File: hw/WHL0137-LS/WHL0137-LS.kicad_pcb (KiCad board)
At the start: 2 copper layers, 109.4 x 133.5 mm, 91 parts, among them J1 Conn_01x05, U1 IS31FL3236A, U2 IS31FL3236A

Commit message: Some floor planning
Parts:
- moved C2 136.4 mm to (-25.4, -62.5), turned to 90 degrees
- moved JP2 128.8 mm to (-20.3, -66.0)
- moved JP1 124.2 mm to (-20.3, -68.6)
- moved C1 111.1 mm to (-11.1, -66.0)
- moved R1 106.8 mm to (-4.72, -54.6)
- moved R2 106.8 mm to (-4.72, -57.6)
- moved R3 76.1 mm to (12.7, -59.7)
- moved R4 73.3 mm to (11.5, -56.9)
- moved C3 71.3 mm to (11.5, -53.3)
- moved TP1 63.1 mm to (5.82, -55.9)
- moved TP2 63.1 mm to (1.27, -55.9)
- moved C4 58.5 mm to (25.4, -62.2), turned to 90 degrees
- moved JP4 57.8 mm to (20.3, -66.0)
- moved R5 32.7 mm to (11.8, -63.5)
- moved D73 28.0 mm to (11.8, -66.0)
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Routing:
- net Net-(U2-Pad40): track 0.00 -> 9.06 mm
- net Net-(U1-Pad40): track 0.00 -> 9.06 mm
- net +5V: track 0.00 -> 5.78 mm, vias 0 -> 3
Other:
- board size 109.4 x 133.5 mm -> 111.5 x 124.3 mm
- copper layers 2 -> 4

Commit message: Some layout
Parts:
- removed R5: 510, Resistor_SMD:R_0805_2012Metric
- R1: value 100k -> 510
- R2: value 3.3k -> 100k
- R3: value 100k -> 3.3k
- moved R3 47.6 mm to (-32.8, -73.7), turned to 90 degrees
- moved TP1 41.4 mm to (-35.6, -55.9)
- moved TP2 41.4 mm to (-40.1, -55.9)
- moved R2 22.7 mm to (-26.7, -63.2), turned to 90 degrees
- moved JP2 21.2 mm to (-4.32, -52.1)
- moved JP1 21.2 mm to (-4.32, -54.6)
- moved JP4 21.1 mm to (4.57, -52.1)
- moved JP3 21.1 mm to (4.57, -54.6)
- moved C2 11.8 mm to (-17.0, -70.9), turned to 0 degrees
- moved C1 6.54 mm to (-17.0, -68.8)
- moved R1 5.18 mm to (-6.60, -59.4), turned to 90 degrees
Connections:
- D1 pad 1: Net-(U1-Pad47) -> Net-(D1-Pad1)
- D2 pad 1: Net-(U1-Pad48) -> Net-(D2-Pad1)
- D28 pad 1: Net-(U1-Pad38) -> Net-(D28-Pad1)
- D29 pad 1: Net-(U1-Pad37) -> Net-(D29-Pad1)
- D3 pad 1: Net-(U1-Pad1) -> Net-(D3-Pad1)
- D37 pad 1: Net-(U2-Pad8) -> Net-(D37-Pad1)
- D38 pad 1: Net-(U2-Pad7) -> Net-(D38-Pad1)
- D39 pad 1: Net-(U2-Pad6) -> Net-(D39-Pad1)
- D4 pad 1: Net-(U1-Pad2) -> Net-(D4-Pad1)
- D40 pad 1: Net-(U2-Pad5) -> Net-(D40-Pad1)
- D41 pad 1: Net-(U2-Pad3) -> Net-(D41-Pad1)
- D42 pad 1: Net-(U2-Pad2) -> Net-(D42-Pad1)
- D43 pad 1: Net-(U2-Pad1) -> Net-(D43-Pad1)
- D44 pad 1: Net-(U2-Pad48) -> Net-(D44-Pad1)
- D45 pad 1: Net-(U2-Pad47) -> Net-(D45-Pad1)
- D5 pad 1: Net-(U1-Pad3) -> Net-(D5-Pad1)
- D6 pad 1: Net-(U1-Pad5) -> Net-(D6-Pad1)
- D7 pad 1: Net-(U1-Pad6) -> Net-(D7-Pad1)
- D8 pad 1: Net-(U1-Pad7) -> Net-(D8-Pad1)
- D9 pad 1: Net-(U1-Pad8) -> Net-(D9-Pad1)
- R1 pad 1: GND -> +5V
- R1 pad 2: /inner_LED_ring/SDB -> Net-(D73-Pad2)
- R2 pad 1: Net-(U1-Pad44) -> /inner_LED_ring/SDB
- R3 pad 1: GND -> Net-(R3-Pad1)
- R3 pad 2: /inner_LED_ring/SDB -> GND
- U1 pad 1: Net-(U1-Pad1) -> Net-(D14-Pad1)
- U1 pad 10: Net-(D11-Pad1) -> Net-(D5-Pad1)
- U1 pad 11: Net-(D12-Pad1) -> Net-(D7-Pad1)
- U1 pad 12: Net-(D13-Pad1) -> Net-(D9-Pad1)
- U1 pad 13: Net-(D14-Pad1) -> Net-(D11-Pad1)
- U1 pad 14: Net-(D15-Pad1) -> Net-(D13-Pad1)
- U1 pad 15: Net-(D16-Pad1) -> Net-(D15-Pad1)
- U1 pad 17: Net-(D18-Pad1) -> Net-(D19-Pad1)
- U1 pad 2: Net-(U1-Pad2) -> Net-(D12-Pad1)
- U1 pad 20: Net-(D19-Pad1) -> Net-(D20-Pad1)
- U1 pad 21: Net-(D20-Pad1) -> Net-(D22-Pad1)
- U1 pad 22: Net-(D21-Pad1) -> Net-(D24-Pad1)
- U1 pad 23: Net-(D22-Pad1) -> Net-(D26-Pad1)
- U1 pad 24: Net-(D23-Pad1) -> Net-(D28-Pad1)
- U1 pad 25: Net-(D24-Pad1) -> Net-(D30-Pad1)
- U1 pad 26: Net-(D25-Pad1) -> Net-(D32-Pad1)
- U1 pad 27: Net-(D26-Pad1) -> Net-(D34-Pad1)
- U1 pad 28: Net-(D27-Pad1) -> Net-(D36-Pad1)
- U1 pad 29: Net-(D36-Pad1) -> Net-(D37-Pad1)
- U1 pad 3: Net-(U1-Pad3) -> Net-(D10-Pad1)
- U1 pad 31: Net-(D34-Pad1) -> Net-(D33-Pad1)
- U1 pad 32: Net-(D33-Pad1) -> Net-(D31-Pad1)
- U1 pad 34: Net-(D32-Pad1) -> Net-(D29-Pad1)
- U1 pad 35: Net-(D31-Pad1) -> Net-(D27-Pad1)
- U1 pad 36: Net-(D30-Pad1) -> Net-(D25-Pad1)
- U1 pad 37: Net-(U1-Pad37) -> Net-(D23-Pad1)
- U1 pad 38: Net-(U1-Pad38) -> Net-(D21-Pad1)
- U1 pad 44: Net-(U1-Pad44) -> Net-(R3-Pad1)
- U1 pad 47: Net-(U1-Pad47) -> Net-(D18-Pad1)
- U1 pad 48: Net-(U1-Pad48) -> Net-(D16-Pad1)
- U1 pad 5: Net-(U1-Pad5) -> Net-(D8-Pad1)
- U1 pad 6: Net-(U1-Pad6) -> Net-(D6-Pad1)
- U1 pad 7: Net-(U1-Pad7) -> Net-(D4-Pad1)
- U1 pad 8: Net-(U1-Pad8) -> Net-(D2-Pad1)
- U1 pad 9: Net-(D10-Pad1) -> Net-(D3-Pad1)
- U2 pad 1: Net-(U2-Pad1) -> Net-(D50-Pad1)
- U2 pad 10: Net-(D47-Pad1) -> Net-(D41-Pad1)
- U2 pad 11: Net-(D48-Pad1) -> Net-(D43-Pad1)
- U2 pad 12: Net-(D49-Pad1) -> Net-(D45-Pad1)
- U2 pad 13: Net-(D50-Pad1) -> Net-(D47-Pad1)
- U2 pad 14: Net-(D51-Pad1) -> Net-(D49-Pad1)
- U2 pad 15: Net-(D52-Pad1) -> Net-(D51-Pad1)
- U2 pad 17: Net-(D54-Pad1) -> Net-(D55-Pad1)
- U2 pad 2: Net-(U2-Pad2) -> Net-(D48-Pad1)
- U2 pad 20: Net-(D55-Pad1) -> Net-(D56-Pad1)
- U2 pad 21: Net-(D56-Pad1) -> Net-(D58-Pad1)
- U2 pad 22: Net-(D57-Pad1) -> Net-(D60-Pad1)
- U2 pad 23: Net-(D58-Pad1) -> Net-(D62-Pad1)
- U2 pad 24: Net-(D59-Pad1) -> Net-(D64-Pad1)
- U2 pad 25: Net-(D60-Pad1) -> Net-(D66-Pad1)
- U2 pad 26: Net-(D61-Pad1) -> Net-(D68-Pad1)
- U2 pad 27: Net-(D62-Pad1) -> Net-(D70-Pad1)
- U2 pad 28: Net-(D63-Pad1) -> Net-(D72-Pad1)
- U2 pad 29: Net-(D64-Pad1) -> Net-(D1-Pad1)
- U2 pad 3: Net-(U2-Pad3) -> Net-(D46-Pad1)
- U2 pad 30: Net-(D65-Pad1) -> Net-(D71-Pad1)
- U2 pad 31: Net-(D66-Pad1) -> Net-(D69-Pad1)
- U2 pad 34: Net-(D68-Pad1) -> Net-(D65-Pad1)
- U2 pad 35: Net-(D69-Pad1) -> Net-(D63-Pad1)
- U2 pad 36: Net-(D70-Pad1) -> Net-(D61-Pad1)
- U2 pad 37: Net-(D71-Pad1) -> Net-(D59-Pad1)
- U2 pad 38: Net-(D72-Pad1) -> Net-(D57-Pad1)
- U2 pad 47: Net-(U2-Pad47) -> Net-(D54-Pad1)
- U2 pad 48: Net-(U2-Pad48) -> Net-(D52-Pad1)
- U2 pad 5: Net-(U2-Pad5) -> Net-(D44-Pad1)
- U2 pad 6: Net-(U2-Pad6) -> Net-(D42-Pad1)
- U2 pad 7: Net-(U2-Pad7) -> Net-(D40-Pad1)
- U2 pad 8: Net-(U2-Pad8) -> Net-(D38-Pad1)
- U2 pad 9: Net-(D46-Pad1) -> Net-(D39-Pad1)
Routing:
- net Net-(D21-Pad1): track 0.00 -> 14.2 mm
- net Net-(D23-Pad1): track 0.00 -> 11.7 mm
- net Net-(D25-Pad1): track 0.00 -> 9.07 mm
- net Net-(JP3-Pad2): track 9.06 -> 0.00 mm
- net Net-(JP1-Pad2): track 9.06 -> 0.00 mm
- net Net-(D27-Pad1): track 0.00 -> 8.28 mm
- net Net-(D5-Pad1): track 0.00 -> 8.07 mm
- net Net-(D29-Pad1): track 0.00 -> 7.49 mm
- net Net-(D4-Pad1): track 0.00 -> 6.90 mm
- net Net-(D31-Pad1): track 0.00 -> 6.50 mm
- net Net-(D2-Pad1): track 0.00 -> 6.32 mm
- net /inner_LED_ring/SCL: track 0.00 -> 5.95 mm
- net +5V: track 5.78 -> 0.00 mm, vias 3 -> 0
- net Net-(D33-Pad1): track 0.00 -> 5.71 mm
- net /inner_LED_ring/SDA: track 0.00 -> 5.56 mm
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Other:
- board size 111.5 x 124.3 mm -> 153.8 x 153.8 mm

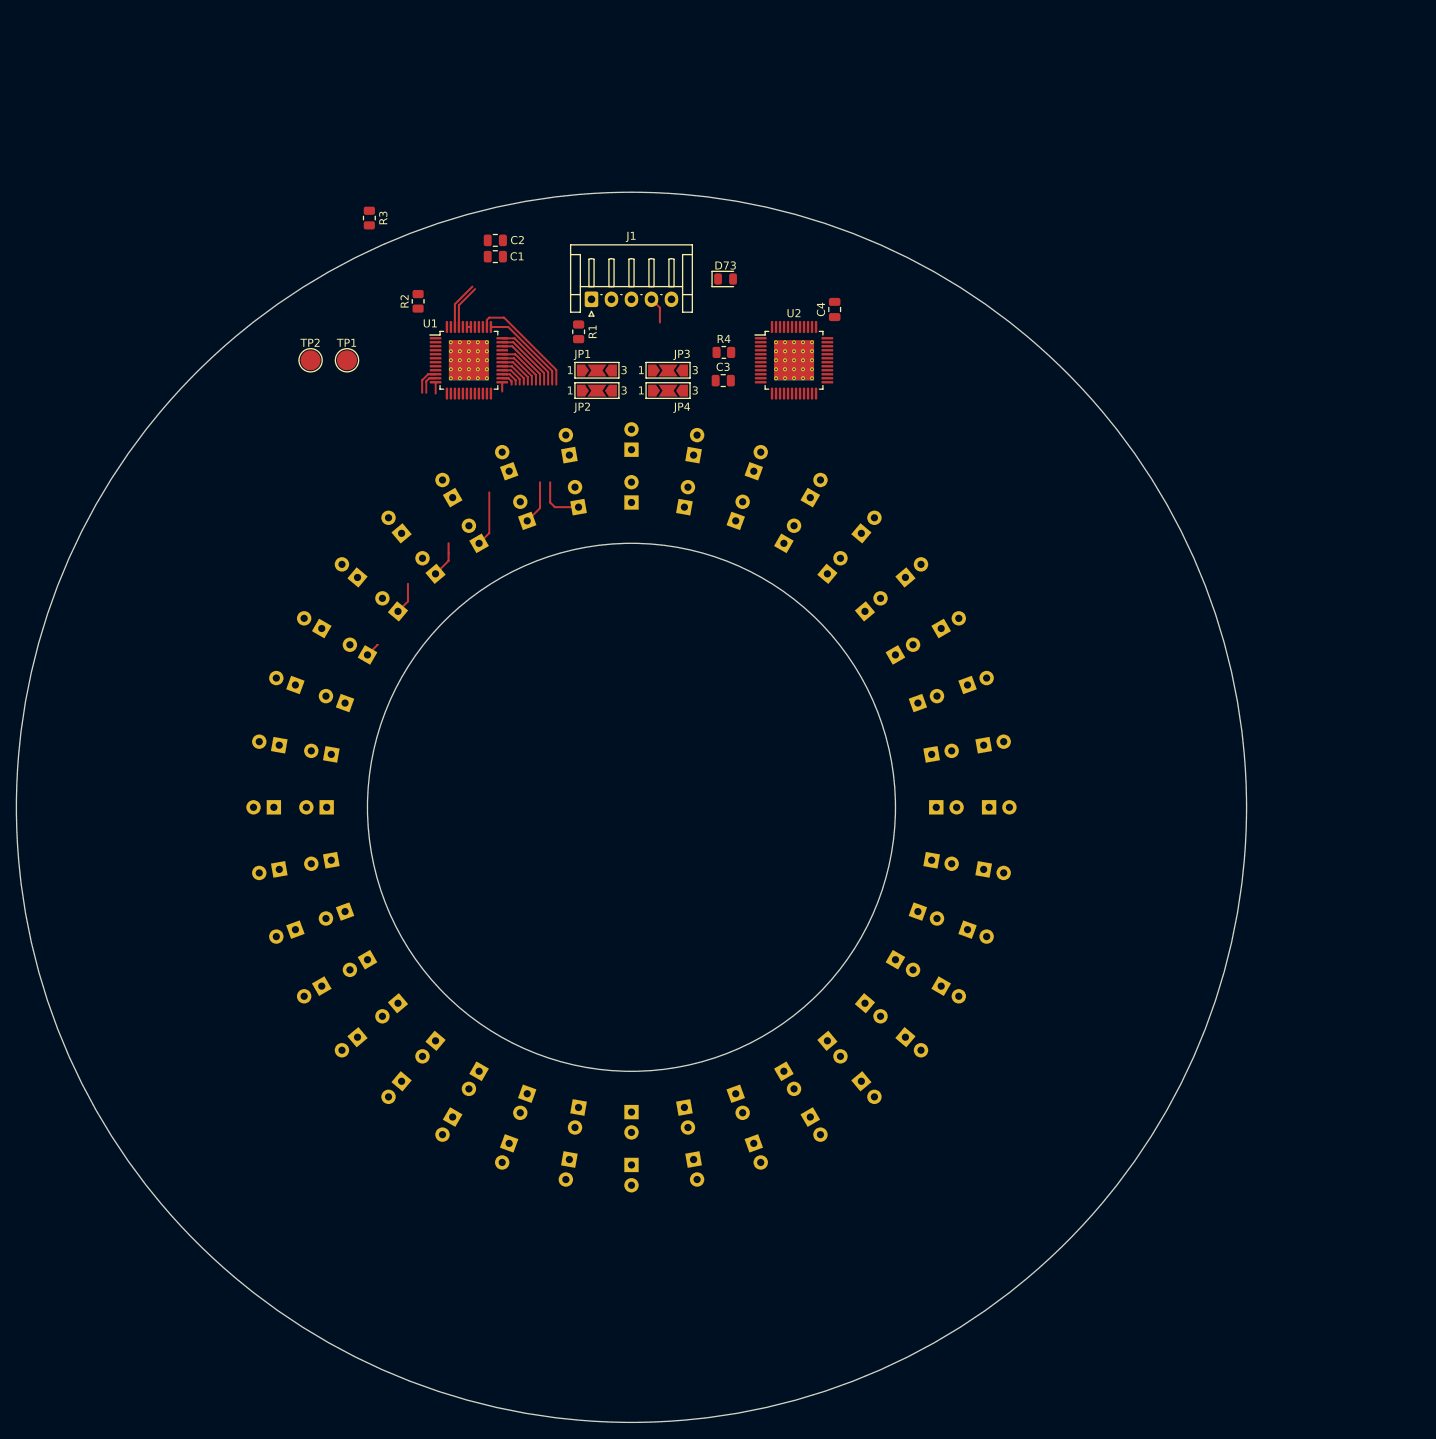
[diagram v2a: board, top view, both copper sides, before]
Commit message: Routed LED traces and fixed designators
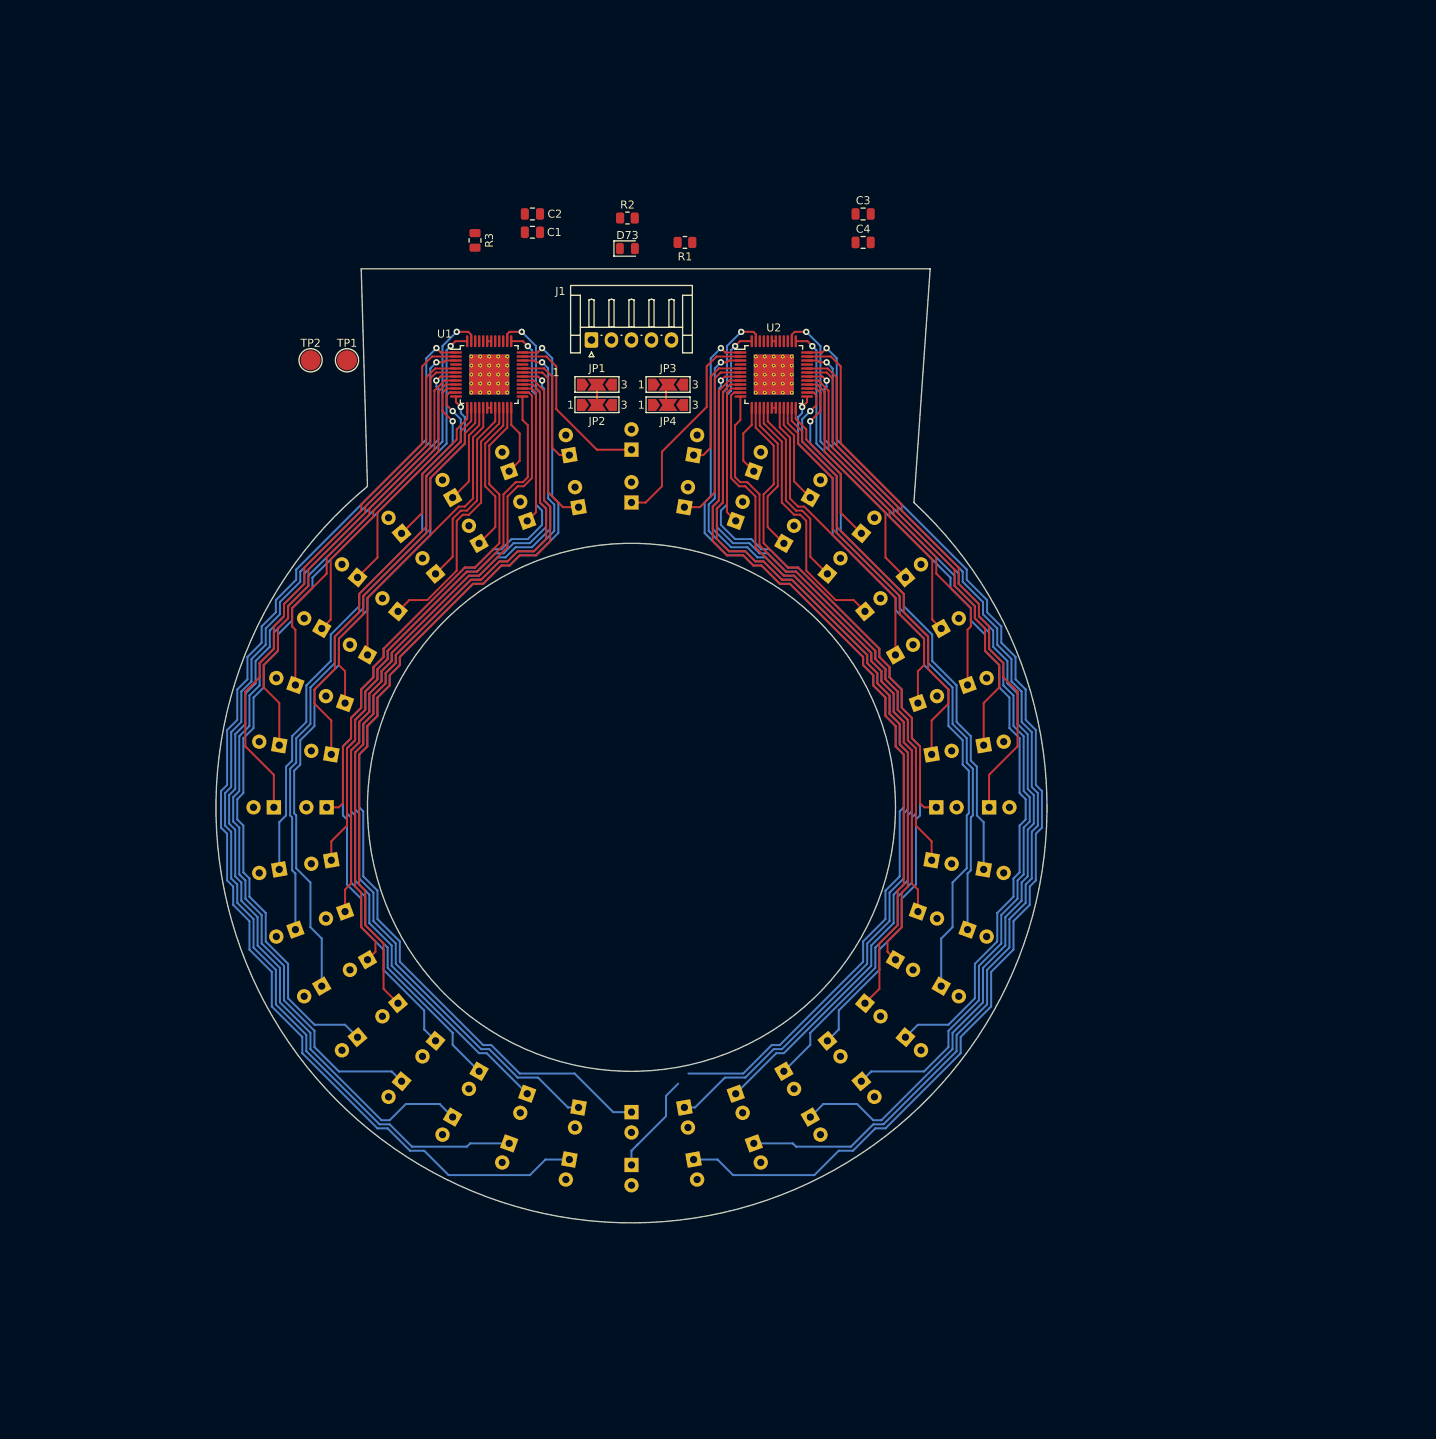
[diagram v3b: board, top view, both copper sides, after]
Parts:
- removed R4: 3.3k, Resistor_SMD:R_0805_2012Metric
- R1: value 510 -> 3.3k
- R2: value 100k -> 510
- moved R2 28.2 mm to (-0.51, -73.7), turned to 0 degrees
- moved C3 27.2 mm to (29.0, -74.2)
- moved R1 17.4 mm to (6.68, -70.6), turned to 0 degrees
- moved R3 13.5 mm to (-19.6, -70.9)
- moved D73 12.8 mm to (-0.51, -69.8)
- moved C4 9.11 mm to (29.0, -70.6), turned to 0 degrees
- moved C2 5.69 mm to (-12.4, -74.2)
- moved C1 5.55 mm to (-12.4, -71.9)
- moved J1 5.08 mm to (-5.00, -58.4)
- moved U1 3.10 mm to (-17.8, -54.1)
- moved U2 3.10 mm to (17.8, -54.1)
- moved JP1 1.78 mm to (-4.32, -52.8)
- moved JP2 1.78 mm to (-4.32, -50.3)
- moved JP3 1.78 mm to (4.57, -52.8)
- moved JP4 1.78 mm to (4.57, -50.3)
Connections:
- net /inner_LED_ring/SCL renamed /led_driver_1/SCL
- net /inner_LED_ring/SDA renamed /led_driver_1/SDA
- net Net-(JP1-Pad2) renamed /led_driver_1/AD
- net Net-(JP3-Pad2) renamed /led_driver_2/AD
- net Net-(R3-Pad1) renamed /led_driver_1/R_EXT
- J1 pad 4: /inner_LED_ring/SDB -> /led_driver_1/SDB
- R1 pad 1: +5V -> /led_driver_2/R_EXT
- R1 pad 2: Net-(D73-Pad2) -> GND
- R2 pad 1: /inner_LED_ring/SDB -> +5V
- R2 pad 2: GND -> Net-(D73-Pad2)
- U1 pad 1: Net-(D14-Pad1) -> Net-(D54-Pad1)
- U1 pad 10: Net-(D5-Pad1) -> Net-(D47-Pad1)
- U1 pad 11: Net-(D7-Pad1) -> Net-(D48-Pad1)
- U1 pad 12: Net-(D9-Pad1) -> Net-(D49-Pad1)
- U1 pad 13: Net-(D11-Pad1) -> Net-(D41-Pad1)
- U1 pad 14: Net-(D13-Pad1) -> Net-(D9-Pad1)
- U1 pad 15: Net-(D15-Pad1) -> Net-(D8-Pad1)
- U1 pad 16: Net-(D17-Pad1) -> Net-(D40-Pad1)
- U1 pad 17: Net-(D19-Pad1) -> Net-(D7-Pad1)
- U1 pad 2: Net-(D12-Pad1) -> Net-(D46-Pad1)
- U1 pad 20: Net-(D20-Pad1) -> Net-(D5-Pad1)
- U1 pad 21: Net-(D22-Pad1) -> Net-(D6-Pad1)
- U1 pad 22: Net-(D24-Pad1) -> Net-(D4-Pad1)
- U1 pad 23: Net-(D26-Pad1) -> Net-(D10-Pad1)
- U1 pad 24: Net-(D28-Pad1) -> Net-(D39-Pad1)
- U1 pad 25: Net-(D30-Pad1) -> Net-(D11-Pad1)
- U1 pad 26: Net-(D32-Pad1) -> Net-(D12-Pad1)
- U1 pad 27: Net-(D34-Pad1) -> Net-(D3-Pad1)
- U1 pad 28: Net-(D36-Pad1) -> Net-(D13-Pad1)
- U1 pad 29: Net-(D37-Pad1) -> Net-(D14-Pad1)
- U1 pad 3: Net-(D10-Pad1) -> Net-(D53-Pad1)
- U1 pad 30: Net-(D35-Pad1) -> Net-(D17-Pad1)
- U1 pad 31: Net-(D33-Pad1) -> Net-(D2-Pad1)
- U1 pad 32: Net-(D31-Pad1) -> Net-(D38-Pad1)
- U1 pad 34: Net-(D29-Pad1) -> Net-(D18-Pad1)
- U1 pad 35: Net-(D27-Pad1) -> Net-(D37-Pad1)
- U1 pad 36: Net-(D25-Pad1) -> Net-(D19-Pad1)
- U1 pad 37: Net-(D23-Pad1) -> Net-(D15-Pad1)
- U1 pad 38: Net-(D21-Pad1) -> Net-(D16-Pad1)
- U1 pad 39: /inner_LED_ring/SDB -> /led_driver_1/SDB
- U1 pad 47: Net-(D18-Pad1) -> Net-(D51-Pad1)
- U1 pad 48: Net-(D16-Pad1) -> Net-(D50-Pad1)
- U1 pad 5: Net-(D8-Pad1) -> Net-(D45-Pad1)
- U1 pad 6: Net-(D6-Pad1) -> Net-(D44-Pad1)
- U1 pad 7: Net-(D4-Pad1) -> Net-(D52-Pad1)
- U1 pad 8: Net-(D2-Pad1) -> Net-(D43-Pad1)
- U1 pad 9: Net-(D3-Pad1) -> Net-(D42-Pad1)
- U2 pad 1: Net-(D50-Pad1) -> Net-(D55-Pad1)
- U2 pad 10: Net-(D41-Pad1) -> Net-(D35-Pad1)
- U2 pad 11: Net-(D43-Pad1) -> Net-(D26-Pad1)
- U2 pad 12: Net-(D45-Pad1) -> Net-(D27-Pad1)
- U2 pad 13: Net-(D47-Pad1) -> Net-(D71-Pad1)
- U2 pad 14: Net-(D49-Pad1) -> Net-(D28-Pad1)
- U2 pad 15: Net-(D51-Pad1) -> Net-(D34-Pad1)
- U2 pad 16: Net-(D53-Pad1) -> Net-(D32-Pad1)
- U2 pad 17: Net-(D55-Pad1) -> Net-(D33-Pad1)
- U2 pad 2: Net-(D48-Pad1) -> Net-(D1-Pad1)
- U2 pad 20: Net-(D56-Pad1) -> Net-(D31-Pad1)
- U2 pad 21: Net-(D58-Pad1) -> Net-(D70-Pad1)
- U2 pad 22: Net-(D60-Pad1) -> Net-(D30-Pad1)
- U2 pad 23: Net-(D62-Pad1) -> Net-(D29-Pad1)
- U2 pad 24: Net-(D64-Pad1) -> Net-(D69-Pad1)
- U2 pad 25: Net-(D66-Pad1) -> Net-(D61-Pad1)
- U2 pad 26: Net-(D68-Pad1) -> Net-(D62-Pad1)
- U2 pad 27: Net-(D70-Pad1) -> Net-(D63-Pad1)
- U2 pad 28: Net-(D72-Pad1) -> Net-(D68-Pad1)
- U2 pad 29: Net-(D1-Pad1) -> Net-(D67-Pad1)
- U2 pad 3: Net-(D46-Pad1) -> Net-(D20-Pad1)
- U2 pad 30: Net-(D71-Pad1) -> Net-(D58-Pad1)
- U2 pad 31: Net-(D69-Pad1) -> Net-(D66-Pad1)
- U2 pad 32: Net-(D67-Pad1) -> Net-(D65-Pad1)
- U2 pad 34: Net-(D65-Pad1) -> Net-(D57-Pad1)
- U2 pad 35: Net-(D63-Pad1) -> Net-(D64-Pad1)
- U2 pad 36: Net-(D61-Pad1) -> Net-(D56-Pad1)
- U2 pad 37: Net-(D59-Pad1) -> Net-(D60-Pad1)
- U2 pad 38: Net-(D57-Pad1) -> Net-(D59-Pad1)
- U2 pad 39: /inner_LED_ring/SDB -> /led_driver_1/SDB
- U2 pad 44: Net-(R4-Pad1) -> /led_driver_2/R_EXT
- U2 pad 47: Net-(D54-Pad1) -> Net-(D22-Pad1)
- U2 pad 48: Net-(D52-Pad1) -> Net-(D23-Pad1)
- U2 pad 5: Net-(D44-Pad1) -> Net-(D72-Pad1)
- U2 pad 6: Net-(D42-Pad1) -> Net-(D36-Pad1)
- U2 pad 7: Net-(D40-Pad1) -> Net-(D21-Pad1)
- U2 pad 8: Net-(D38-Pad1) -> Net-(D24-Pad1)
- U2 pad 9: Net-(D39-Pad1) -> Net-(D25-Pad1)
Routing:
- net Net-(D56-Pad1): track 0.00 -> 146.7 mm, vias 0 -> 1
- net Net-(D54-Pad1): track 0.00 -> 146.7 mm
- net Net-(D55-Pad1): track 0.00 -> 135.4 mm
- net Net-(D57-Pad1): track 0.00 -> 134.3 mm, vias 0 -> 1
- net Net-(D53-Pad1): track 0.00 -> 134.3 mm
- net Net-(D19-Pad1): track 0.00 -> 131.9 mm, vias 0 -> 1
- net Net-(D58-Pad1): track 0.00 -> 124.4 mm, vias 0 -> 1
- net Net-(D52-Pad1): track 0.00 -> 124.4 mm, vias 0 -> 2
- net Net-(D20-Pad1): track 0.00 -> 123.6 mm
- net Net-(D18-Pad1): track 0.00 -> 123.6 mm, vias 0 -> 1
- net Net-(D59-Pad1): track 0.00 -> 120.6 mm, vias 0 -> 1
- net Net-(D51-Pad1): track 0.00 -> 120.6 mm, vias 0 -> 1
- net Net-(D22-Pad1): track 0.00 -> 116.2 mm, vias 0 -> 1
- net Net-(D16-Pad1): track 0.00 -> 116.2 mm, vias 0 -> 1
- net Net-(D17-Pad1): track 0.00 -> 114.7 mm, vias 0 -> 1
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- added copper zone on In1.Cu, net +5V
- added copper zone on In2.Cu, net +5V
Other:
- board size 153.8 x 153.8 mm -> 103.9 x 119.3 mm

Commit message: More layout progress
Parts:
- moved C3 14.6 mm to (21.8, -61.5)
- moved R2 13.8 mm to (-9.91, -63.5)
- moved C2 13.7 mm to (-21.3, -63.8), turned to 180 degrees
- moved C1 13.5 mm to (-21.3, -61.7), turned to 180 degrees
- moved D73 12.2 mm to (9.91, -63.5), turned to 180 degrees
- moved R1 12.0 mm to (16.5, -63.8), turned to 180 degrees
- moved C4 10.1 mm to (21.8, -63.5)
- moved TP2 9.90 mm to (-30.2, -56.4)
- moved R3 7.55 mm to (-17.0, -63.8), turned to 180 degrees
- moved TP1 7.54 mm to (-30.2, -61.2)
- moved JP3 2.90 mm to (1.78, -52.1), turned to 90 degrees
- moved JP2 2.90 mm to (-2.03, -52.1), turned to 90 degrees
- moved JP4 2.34 mm to (6.10, -52.1), turned to 90 degrees
- moved JP1 2.17 mm to (-6.35, -52.1), turned to 90 degrees
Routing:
- net /led_driver_1/SDA: track 0.00 -> 64.8 mm
- net /led_driver_1/SCL: track 0.00 -> 55.8 mm, vias 0 -> 1
- net /led_driver_1/SDB: track 0.00 -> 43.9 mm, vias 0 -> 2
- net /led_driver_2/AD: track 2.54 -> 27.2 mm, vias 0 -> 2
- net /led_driver_1/AD: track 2.54 -> 24.4 mm, vias 0 -> 2
- net +5V: track 0.00 -> 18.5 mm, vias 0 -> 7
- net Net-(D73-Pad2): track 0.00 -> 18.0 mm
- net GND: track 2.00 -> 14.1 mm, vias 0 -> 7
- net /led_driver_1/R_EXT: track 0.00 -> 8.65 mm, vias 0 -> 2
- net /led_driver_2/R_EXT: track 0.00 -> 7.74 mm, vias 0 -> 2
- net Net-(D55-Pad1): track 135.4 -> 137.2 mm, vias 0 -> 1
- net Net-(D21-Pad1): vias 0 -> 1
- net Net-(D54-Pad1): vias 0 -> 1
- net Net-(D53-Pad1): vias 0 -> 1
- net Net-(D52-Pad1): vias 2 -> 1
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- added copper zone on In1.Cu, net GND
- removed copper zone on In1.Cu, net +5V
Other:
- board size 103.9 x 119.3 mm -> 103.9 x 117.2 mm
